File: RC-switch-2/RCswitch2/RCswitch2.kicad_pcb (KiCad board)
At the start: 2 copper layers, 10 parts, among them J1 Conn_01x03, J2 Conn_01x02, J3 Conn_01x02, J4 Conn_01x02, U1 4013, U2 PVG612

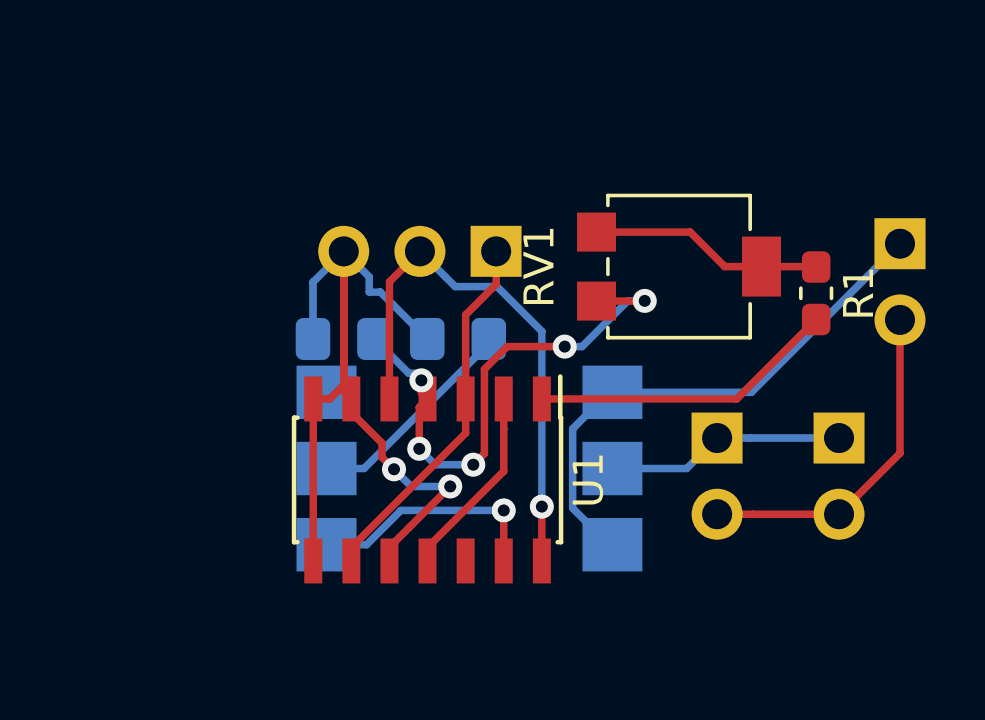
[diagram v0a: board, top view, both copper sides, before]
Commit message: Done with RCswitch2. Production is ordered from JLCPCB
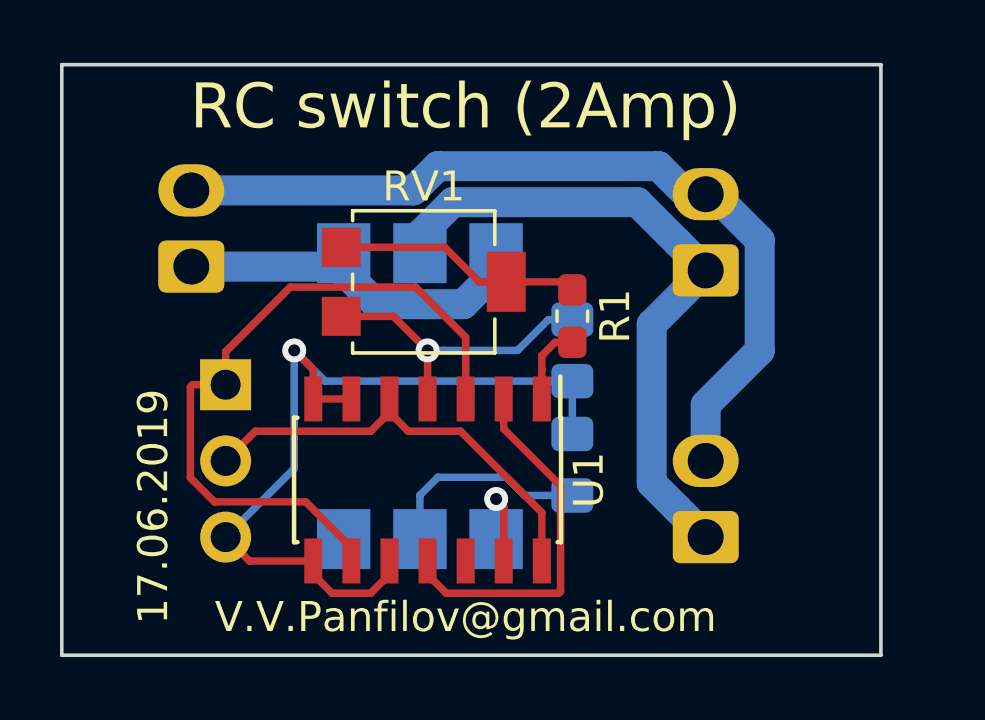
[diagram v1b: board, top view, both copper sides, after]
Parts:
- J1: footprint Connector_PinSocket_2.54mm:PinSocket_1x03_P2.54mm_Vertical -> Connector_PinHeader_2.54mm:PinHeader_1x03_P2.54mm_Vertical
- J2, J3, J4: footprint Connector_PinSocket_2.54mm:PinSocket_1x02_P2.54mm_Vertical -> Connector_Molex:Molex_KK-254_AE-6410-02A_1x02_P2.54mm_Vertical
- moved J2 23.6 mm to (30.1, 45.3), turned to 90 degrees
- moved J1 10.1 mm to (31.2, 49.3), turned to 180 degrees
- moved RV1 8.52 mm to (37.8, 45.8)
- moved R1 8.16 mm to (42.8, 47.0)
- moved C1 7.63 mm to (42.8, 48.1), turned to 270 degrees
- moved J4 7.14 mm to (47.2, 45.5), turned to 90 degrees
- moved R2 5.66 mm to (42.8, 51.9), turned to 90 degrees
- moved J3 3.32 mm to (47.2, 54.4), turned to 90 degrees
- moved U2 2.92 mm to (37.7, 49.7), turned to 90 degrees
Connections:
- net Net-(J2-Pad1) renamed /Power1
- net Net-(J2-Pad2) renamed /Power3
- net Net-(J3-Pad1) renamed /Power2
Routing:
- net /Power3: track 11.4 -> 28.4 mm
- net /Power2: track 7.97 -> 21.9 mm
- net Net-(J1-Pad1): track 12.3 -> 23.8 mm
- net Net-(C1-Pad1): track 17.8 -> 10.2 mm, vias 5 -> 1
- net Net-(R1-Pad2): track 10.2 -> 2.64 mm
- net Net-(U1-Pad11): track 6.45 -> 12.4 mm
- net /Power1: track 17.9 -> 12.5 mm
- net Net-(U1-Pad13): track 8.07 -> 3.77 mm
- net GND: track 32.1 -> 29.0 mm, vias 2 -> 1
- net Net-(J1-Pad2): track 18.2 -> 15.1 mm, vias 1 -> 0
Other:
- board outline added: 27.3 x 19.7 mm
- net class Power added: clearance 0.2, trace_width 1, via_dia 0.8, via_drill 0.4
- board text added: "+"
- board text added: "17.06.2019"
- board text added: "IN"
- board text added: "INPUT"
- board text added: "OUTPUT"
- board text added: "RC switch (2Amp)"
- board text added: "V.V.Panfilov@gmail.com"
- board text added: "ppm + gnd"

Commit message: Added old RCSwitch-2 project for my friend S.Koslovsky
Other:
- net class Default removed
- net class Power removed
